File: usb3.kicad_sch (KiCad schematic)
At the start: 45 parts, among them J5 WE_632723300011_alt_symbol, Q4 NX138BKMYL, U17 HD3SS3220, U18 AP22615, U19 TPD4E05U06QDQARQ1, U20 TPD4E05U06QDQARQ1, U21 TPD4E05U06QDQARQ1

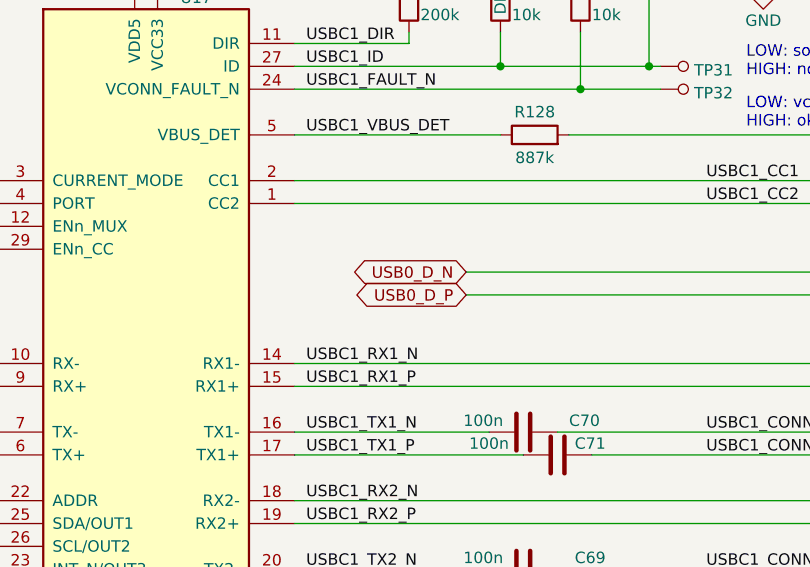
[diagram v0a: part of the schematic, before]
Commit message: Routed USB 2.0; Routed 5V and 3V3 power rails
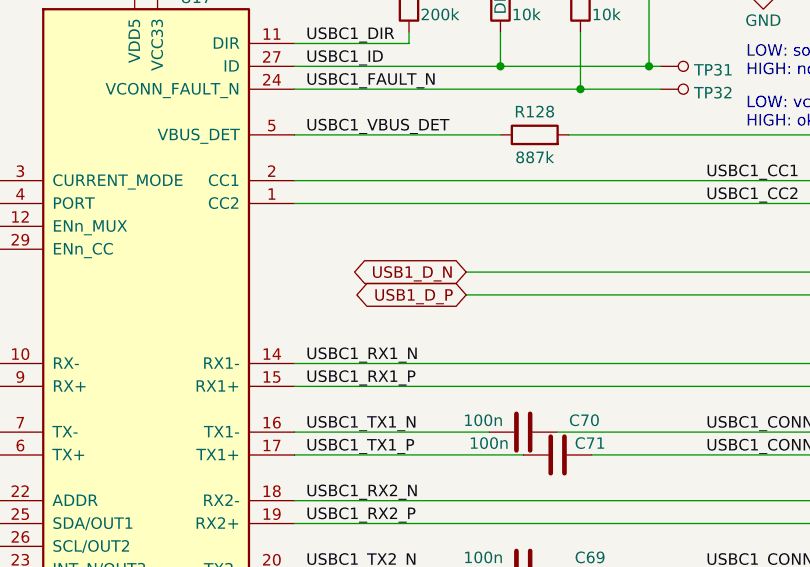
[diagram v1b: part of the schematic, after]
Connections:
- net USB0_D_N renamed USB1_D_N
- net USB0_D_P renamed USB1_D_P
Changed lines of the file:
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@@
-    )
-  )
-  (global_label "USB0_D_P" (shape bidirectional) (at 195.58 147.32 180)
-    (effects (font (size 1.27 1.27)) (justify right))
-    (property "Intersheet References" "${INTERSHEET_REFS}" (id 0) (at 182.245 147.32 0)
-      (effects (font (size 1.1 1.1)) (justify right))
-    )
-  )
-  (global_label "USB0_D_N" (shape bidirectional) (at 195.58 144.78 180)
-    (effects (font (size 1.27 1.27)) (justify right))
-    (property "Intersheet References" "${INTERSHEET_REFS}" (id 0) (at 182.245 144.78 0)
-      (effects (font (size 1.1 1.1)) (justify right))
     )
   )
@@
     )
   )
+  (global_label "USB1_D_N" (shape bidirectional) (at 195.58 144.78 180)
+    (effects (font (size 1.27 1.27)) (justify right))
+    (property "Intersheet References" "${INTERSHEET_REFS}" (id 0) (at 181.5576 144.78 0)
+      (effects (font (size 1.1 1.1)) (justify right))
+    )
+  )
   (global_label "USBSS2_RX_N" (shape output) (at 95.25 154.94 180)
     (effects (font (size 1.27 1.27)) (justify right))
@@
       (effects (font (size 1.1 1.1)) (justify right))
     )
+  )
+  (global_label "USB1_D_P" (shape bidirectional) (at 195.58 147.32 180)
+    (effects (font (size 1.27 1.27)) (justify right))
+    (property "Intersheet References" "${INTERSHEET_REFS}" (id 0) (at 181.61 147.32 0)
+      (effects (font (size 1.1 1.1)) (justify right))
+    )

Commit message: Loclib
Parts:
- C66, C74: footprint antmicro-footprints:0603-cap -> jetson-orin-baseboard-footprints:0603-cap; symbol antmicroCapacitors0603:C_10u_0603 -> jetson-orin-baseboard:C_10u_0603
- C67, C68, C69, C70, C71, C72, C73, C75, C86, C87, C88, C92: footprint antmicro-footprints:0402-cap -> jetson-orin-baseboard-footprints:0402-cap; symbol antmicroCapacitors0402:C_100n_0402 -> jetson-orin-baseboard:C_100n_0402
- D10: footprint antmicro-footprints:SOD-923 -> jetson-orin-baseboard-footprints:SOD-923; symbol antmicroTVSDiodes:ESD9X5.0ST5G -> jetson-orin-baseboard:ESD9X5.0ST5G
- D11: footprint antmicro-footprints:LED_0603 -> jetson-orin-baseboard-footprints:LED_0603; symbol antmicroLEDIndicationDiscrete:LTST-C190GKT -> jetson-orin-baseboard:LTST-C190GKT
- J5: footprint antmicro-footprints:WE_632723300011 -> jetson-orin-baseboard-footprints:WE_632723300011; symbol antmicroUSBDVIHDMIConnectors:WE_632723300011_alt_symbol -> jetson-orin-baseboard:WE_632723300011_alt_symbol
- Q4: footprint antmicro-footprints:DFN1006-3 -> jetson-orin-baseboard-footprints:DFN1006-3; symbol antmicroTransistorsFETsMOSFETsSingle:NX138BKMYL -> jetson-orin-baseboard:NX138BKMYL
- R113, R114, R118, R119, R124, R125: footprint antmicro-footprints:0402-res -> jetson-orin-baseboard-footprints:0402-res; symbol antmicroResistors0402:R_0R_0402 -> jetson-orin-baseboard:R_0R_0402
- R115, R116, R117, R127, R135, R136, R137, R138: footprint antmicro-footprints:0402-res -> jetson-orin-baseboard-footprints:0402-res; symbol antmicroResistors0402:R_10k_0402 -> jetson-orin-baseboard:R_10k_0402
- R126: footprint antmicro-footprints:0402-res -> jetson-orin-baseboard-footprints:0402-res; symbol antmicroResistors0402:R_200k_0402 -> jetson-orin-baseboard:R_200k_0402
- R128: footprint antmicro-footprints:0402-res -> jetson-orin-baseboard-footprints:0402-res; symbol antmicroResistors0402:R_887k_0402 -> jetson-orin-baseboard:R_887k_0402
- R139: footprint antmicro-footprints:0402-res -> jetson-orin-baseboard-footprints:0402-res; symbol antmicroResistors0402:R_2k2_0402 -> jetson-orin-baseboard:R_2k2_0402
- R140: footprint antmicro-footprints:0402-res -> jetson-orin-baseboard-footprints:0402-res; symbol antmicroResistors0402:R_470R_0402 -> jetson-orin-baseboard:R_470R_0402
- TP30, TP31, TP32, TP33: footprint antmicro-footprints:Testpoint_smd_0_75mm -> jetson-orin-baseboard-footprints:Testpoint_smd_0_75mm; symbol antmicroTestPoints:TP_SMD_0_75MM -> jetson-orin-baseboard:TP_SMD_0_75MM
- U17: footprint antmicro-footprints:RNH0030A -> jetson-orin-baseboard-footprints:RNH0030A; symbol antmicroInterfaceControllers:HD3SS3220 -> jetson-orin-baseboard:HD3SS3220
- U18: footprint antmicro-footprints:TSOT23-6 -> jetson-orin-baseboard-footprints:TSOT23-6; symbol antmicroPMICPowerDistributionSwitchesLoadDrivers:AP22615 -> jetson-orin-baseboard:AP22615
- U19, U20, U21: footprint antmicro-footprints:USON-10_2.5x1.0mm_P0.5mm -> jetson-orin-baseboard-footprints:USON-10_2.5x1.0mm_P0.5mm; symbol antmicroTVSDiodes:TPD4E05U06QDQARQ1 -> jetson-orin-baseboard:TPD4E05U06QDQARQ1
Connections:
- net +3V3: no longer U17.8 (VCC33)
- net +5V: no longer U17.30 (VDD5), U18.6 (IN)
- net GND: no longer U17.13 (GND), U17.28 (GND), U17.31 (GND), U18.2 (GND), U20.3 (GND), U20.8 (GND)
- net USBC1_ADDR: no longer U17.22 (ADDR)
- net USBC1_CC1: no longer U17.2 (CC1)
- net USBC1_CC2: no longer U17.1 (CC2)
- net USBC1_CONN_TX1_N: no longer U20.4 (IO3), U20.7 (IO3)
- net USBC1_CONN_TX1_P: no longer U20.5 (IO4), U20.6 (IO4)
- net USBC1_DIR: no longer U17.11 (DIR)
- net USBC1_FAULT_N: no longer U17.24 (VCONN_FAULT_N)
- net USBC1_I2C_SDA: no longer U17.25 (SDA/OUT1)
- net USBC1_ID: no longer U17.27 (ID)
- net USBC1_ISC_SCL: no longer U17.26 (SCL/OUT2)
- net USBC1_ISET: no longer U18.5 (ISET)
- net USBC1_I_MODE: no longer U17.3 (CURRENT_MODE)
- net USBC1_PORT: no longer U17.4 (PORT)
- net USBC1_RX1_N: no longer U17.14 (RX1-), U20.1 (IO1), U20.10 (IO1)
- net USBC1_RX1_P: no longer U17.15 (RX1+), U20.2 (IO2), U20.9 (IO2)
- net USBC1_RX2_N: no longer U17.18 (RX2-)
- net USBC1_RX2_P: no longer U17.19 (RX2+)
- net USBC1_TX1_N: no longer U17.16 (TX1-)
- net USBC1_TX1_P: no longer U17.17 (TX1+)
- net USBC1_TX2_N: no longer U17.20 (TX2-)
- net USBC1_TX2_P: no longer U17.21 (TX2+)
- net USBC1_VBUS: no longer U18.1 (OUT)
- net USBC1_VBUS_DET: no longer U17.5 (VBUS_DET)
- net USBSS1_C_RX_N: no longer U17.10 (RX-)
- net USBSS1_C_RX_P: no longer U17.9 (RX+)
- net USBSS1_C_TX_N: no longer U17.7 (TX-)
- net USBSS1_C_TX_P: no longer U17.6 (TX+)
- net ~{USBC1_EN_CC}: no longer U17.29 (ENn_CC)
- net ~{USBC1_EN_MUX}: no longer U17.12 (ENn_MUX)
- net ~{USBC1_INT}: no longer U17.23 (INT_N/OUT3)
- net at R138.1, TP33.1: no longer U18.3 (FLG)
- net at Q4.3 (D), R137.1: no longer U18.4 (EN)

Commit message: Fix symbols after loclib
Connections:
- net +3V3: now also U17.8 (VCC33)
- net +5V: now also U17.30 (VDD5), U18.6 (IN)
- net GND: now also U17.13 (GND), U17.28 (GND), U17.31 (GND), U18.2 (GND), U20.3 (GND), U20.8 (GND)
- net USBC1_ADDR: now also U17.22 (ADDR)
- net USBC1_CC1: now also U17.2 (CC1)
- net USBC1_CC2: now also U17.1 (CC2)
- net USBC1_CONN_TX1_N: now also U20.4 (IO3), U20.7 (IO3)
- net USBC1_CONN_TX1_P: now also U20.5 (IO4), U20.6 (IO4)
- net USBC1_DIR: now also U17.11 (DIR)
- net USBC1_FAULT_N: now also U17.24 (VCONN_FAULT_N)
- net USBC1_I2C_SDA: now also U17.25 (SDA/OUT1)
- net USBC1_ID: now also U17.27 (ID)
- net USBC1_ISC_SCL: now also U17.26 (SCL/OUT2)
- net USBC1_ISET: now also U18.5 (ISET)
- net USBC1_I_MODE: now also U17.3 (CURRENT_MODE)
- net USBC1_PORT: now also U17.4 (PORT)
- net USBC1_RX1_N: now also U17.14 (RX1-), U20.1 (IO1), U20.10 (IO1)
- net USBC1_RX1_P: now also U17.15 (RX1+), U20.2 (IO2), U20.9 (IO2)
- net USBC1_RX2_N: now also U17.18 (RX2-)
- net USBC1_RX2_P: now also U17.19 (RX2+)
- net USBC1_TX1_N: now also U17.16 (TX1-)
- net USBC1_TX1_P: now also U17.17 (TX1+)
- net USBC1_TX2_N: now also U17.20 (TX2-)
- net USBC1_TX2_P: now also U17.21 (TX2+)
- net USBC1_VBUS: now also U18.1 (OUT)
- net USBC1_VBUS_DET: now also U17.5 (VBUS_DET)
- net USBSS1_C_RX_N: now also U17.10 (RX-)
- net USBSS1_C_RX_P: now also U17.9 (RX+)
- net USBSS1_C_TX_N: now also U17.7 (TX-)
- net USBSS1_C_TX_P: now also U17.6 (TX+)
- net ~{USBC1_EN_CC}: now also U17.29 (ENn_CC)
- net ~{USBC1_EN_MUX}: now also U17.12 (ENn_MUX)
- net ~{USBC1_INT}: now also U17.23 (INT_N/OUT3)
- net at R138.1, TP33.1: now also U18.3 (FLG)
- net at Q4.3 (D), R137.1: now also U18.4 (EN)

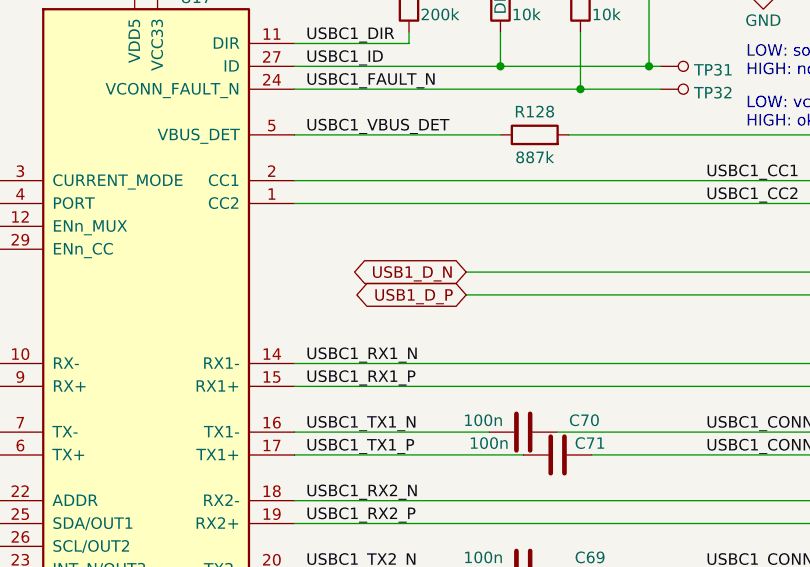
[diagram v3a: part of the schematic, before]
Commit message: Swapped order of USB 2.0 lanes [#40389]
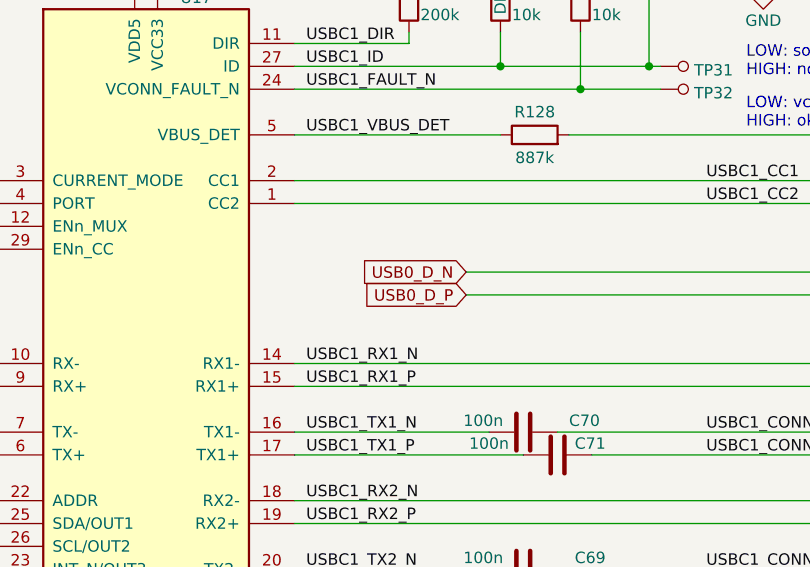
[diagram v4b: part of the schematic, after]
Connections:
- net USB1_D_N renamed USB0_D_N
- net USB1_D_P renamed USB0_D_P
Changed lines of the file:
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@@
+    )
+  )
+  (global_label "USB0_D_N" (shape input) (at 195.58 144.78 180)
+    (effects (font (size 1.27 1.27)) (justify right))
+    (property "Intersheet References" "${INTERSHEET_REFS}" (id 0) (at 182.245 144.78 0)
+      (effects (font (size 1.27 1.27)) (justify right))
     )
   )
@@
     (effects (font (size 1.27 1.27)) (justify right))
     (property "Intersheet References" "${INTERSHEET_REFS}" (id 0) (at 76.835 162.56 0)
+      (effects (font (size 1.27 1.27)) (justify right))
+    )
+  )
+  (global_label "USB0_D_P" (shape input) (at 195.58 147.32 180)
+    (effects (font (size 1.27 1.27)) (justify right))
+    (property "Intersheet References" "${INTERSHEET_REFS}" (id 0) (at 182.245 147.32 0)
       (effects (font (size 1.27 1.27)) (justify right))
     )
@@
     )
   )
-  (global_label "USB1_D_N" (shape bidirectional) (at 195.58 144.78 180)
-    (effects (font (size 1.27 1.27)) (justify right))
-    (property "Intersheet References" "${INTERSHEET_REFS}" (id 0) (at 181.5576 144.78 0)
-      (effects (font (size 1.1 1.1)) (justify right))
-    )
-  )
   (global_label "USBSS2_RX_N" (shape output) (at 95.25 154.94 180)
     (effects (font (size 1.27 1.27)) (justify right))
@@
       (effects (font (size 1.1 1.1)) (justify right))
     )
-  )
-  (global_label "USB1_D_P" (shape bidirectional) (at 195.58 147.32 180)
-    (effects (font (size 1.27 1.27)) (justify right))
-    (property "Intersheet References" "${INTERSHEET_REFS}" (id 0) (at 181.61 147.32 0)
-      (effects (font (size 1.1 1.1)) (justify right))
-    )

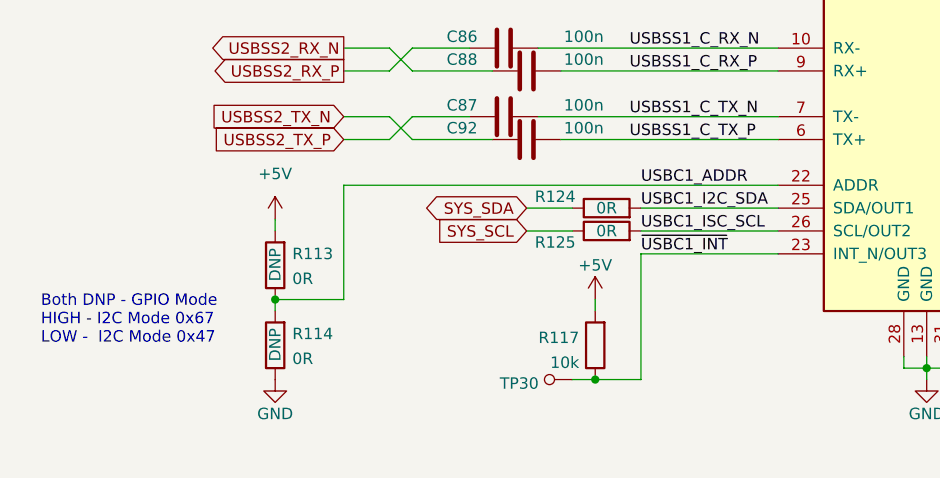
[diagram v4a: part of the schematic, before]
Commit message: Changed default configuration of U17 to I2C [#40390]
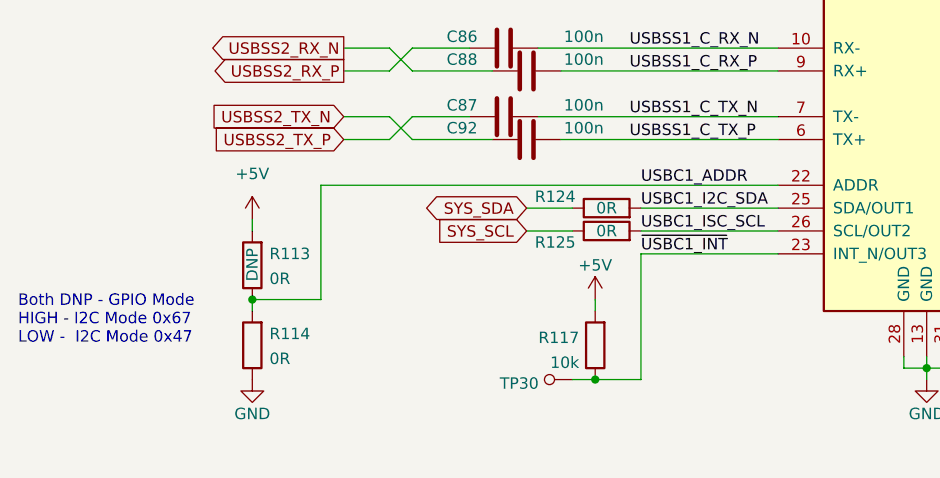
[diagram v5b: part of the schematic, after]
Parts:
- R114: DNP DNP -> (none)
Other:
- moved on the sheet: R113, R114
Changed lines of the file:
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@@
   (junction (at 245.11 177.8) (diameter 0) (color 0 0 0 0)
   )
-  (junction (at 87.63 182.88) (diameter 0) (color 0 0 0 0)
+  (junction (at 85.09 182.88) (diameter 0) (color 0 0 0 0)
   )
   (junction (at 123.19 191.77) (diameter 0) (color 0 0 0 0)
@@
     (stroke (width 0) (type default) (color 0 0 0 0))
   )
-  (wire (pts (xy 87.63 182.88) (xy 87.63 184.15))
+  (wire (pts (xy 85.09 182.88) (xy 85.09 184.15))
     (stroke (width 0) (type default) (color 0 0 0 0))
   )
@@
     (stroke (width 0) (type default) (color 0 0 0 0))
   )
-  (wire (pts (xy 95.25 182.88) (xy 95.25 170.18))
+  (wire (pts (xy 92.71 182.88) (xy 92.71 170.18))
     (stroke (width 0) (type default) (color 0 0 0 0))
   )
@@
     (stroke (width 0) (type default) (color 0 0 0 0))
   )
-  (wire (pts (xy 87.63 182.88) (xy 95.25 182.88))
+  (wire (pts (xy 85.09 182.88) (xy 92.71 182.88))
     (stroke (width 0) (type default) (color 0 0 0 0))
   )
-  (wire (pts (xy 95.25 170.18) (xy 143.51 170.18))
+  (wire (pts (xy 92.71 170.18) (xy 143.51 170.18))
     (stroke (width 0) (type default) (color 0 0 0 0))
   )
@@
     (stroke (width 0) (type default) (color 0 0 0 0))
   )
-  (wire (pts (xy 87.63 173.99) (xy 87.63 175.26))
+  (wire (pts (xy 85.09 173.99) (xy 85.09 175.26))
     (stroke (width 0) (type default) (color 0 0 0 0))
   )
@@
   )
   (text "Both DNP - GPIO Mode\nHIGH - I2C Mode 0x67\nLOW -  I2C Mode 0x47"
-    (at 61.595 187.96 0)
+    (at 59.055 187.96 0)
     (effects (font (size 1.27 1.27)) (justify left bottom))
   )
@@
     (pin "1")
   )
-  (symbol (lib_id "jetson-orin-baseboard:R_0R_0402") (at 87.63 187.96 90) (unit 1)
+  (symbol (lib_id "jetson-orin-baseboard:R_0R_0402") (at 85.09 187.96 90) (unit 1)
     (in_bom yes) (on_board yes)
-    (property "Reference" "R114" (id 0) (at 89.535 186.69 90)
+    (property "Reference" "R114" (id 0) (at 86.995 186.69 90)
       (effects (font (size 1.27 1.27)) (justify right))
     )
-    (property "Value" "R_0R_0402" (id 1) (at 91.44 187.96 0)
+    (property "Value" "R_0R_0402" (id 1) (at 88.9 187.96 0)
       (effects (font (size 1.27 1.27)) hide)
     )
-    (property "Footprint" "jetson-orin-baseboard-footprints:0402-res" (id 2) (at 82.55 182.88 0)
+    (property "Footprint" "jetson-orin-baseboard-footprints:0402-res" (id 2) (at 80.01 182.88 0)
       (effects (font (size 1.524 1.524)) (justify left) hide)
     )
-    (property "Datasheet" "" (id 3) (at 87.63 187.96 0)
+    (property "Datasheet" "" (id 3) (at 85.09 187.96 0)
       (effects (font (size 1.27 1.27)) hide)
     )
-    (property "Manufacturer" "PANASONIC" (id 4) (at 77.47 182.88 0)
+    (property "Manufacturer" "PANASONIC" (id 4) (at 74.93 182.88 0)
       (effects (font (size 1.524 1.524)) (justify left) hide)
     )
-    (property "MPN" "ERJ2GE0R00X" (id 5) (at 80.01 182.88 0)
+    (property "MPN" "ERJ2GE0R00X" (id 5) (at 77.47 182.88 0)
       (effects (font (size 1.524 1.524)) (justify left) hide)
     )
-    (property "Val" "0R" (id 6) (at 89.535 189.4551 90)
-      (effects (font (size 1.27 1.27)) (justify right))
-    )
-    (property "DNP" "DNP" (id 7) (at 87.63 186.055 0)
+    (property "Val" "0R" (id 6) (at 86.995 189.4551 90)
       (effects (font (size 1.27 1.27)) (justify right))
     )
@@
     (pin "1")
   )
-  (symbol (lib_id "jetson-orin-baseboard:GND") (at 87.63 191.77 0) (unit 1)
+  (symbol (lib_id "jetson-orin-baseboard:GND") (at 85.09 191.77 0) (unit 1)
     (in_bom yes) (on_board yes)
-    (property "Reference" "#PWR0109" (id 0) (at 87.63 198.12 0)
+    (property "Reference" "#PWR0109" (id 0) (at 85.09 198.12 0)
       (effects (font (size 1.27 1.27)) hide)
     )
-    (property "Value" "GND" (id 1) (at 87.63 195.58 0))
-    (property "Footprint" "" (id 2) (at 87.63 191.77 0)
+    (property "Value" "GND" (id 1) (at 85.09 195.58 0))
+    (property "Footprint" "" (id 2) (at 85.09 191.77 0)
       (effects (font (size 1.27 1.27)) hide)
     )
-    (property "Datasheet" "" (id 3) (at 87.63 191.77 0)
+    (property "Datasheet" "" (id 3) (at 85.09 191.77 0)
       (effects (font (size 1.27 1.27)) hide)
     )
@@
     (pin "2")
   )
-  (symbol (lib_id "jetson-orin-baseboard:+5V") (at 87.63 173.99 0) (unit 1)
+  (symbol (lib_id "jetson-orin-baseboard:+5V") (at 85.09 173.99 0) (unit 1)
     (in_bom yes) (on_board yes) (fields_autoplaced)
-    (property "Reference" "#PWR0108" (id 0) (at 87.63 177.8 0)
+    (property "Reference" "#PWR0108" (id 0) (at 85.09 177.8 0)
       (effects (font (size 1.27 1.27)) hide)
     )
-    (property "Value" "+5V" (id 1) (at 87.63 168.91 0))
-    (property "Footprint" "" (id 2) (at 87.63 173.99 0)
+    (property "Value" "+5V" (id 1) (at 85.09 168.91 0))
+    (property "Footprint" "" (id 2) (at 85.09 173.99 0)
       (effects (font (size 1.27 1.27)) hide)
     )
-    (property "Datasheet" "" (id 3) (at 87.63 173.99 0)
+    (property "Datasheet" "" (id 3) (at 85.09 173.99 0)
       (effects (font (size 1.27 1.27)) hide)
     )
@@
     (pin "1")
   )
-  (symbol (lib_id "jetson-orin-baseboard:R_0R_0402") (at 87.63 179.07 90) (unit 1)
+  (symbol (lib_id "jetson-orin-baseboard:R_0R_0402") (at 85.09 179.07 90) (unit 1)
     (in_bom yes) (on_board yes)
-    (property "Reference" "R113" (id 0) (at 89.535 177.8 90)
+    (property "Reference" "R113" (id 0) (at 86.995 177.8 90)
       (effects (font (size 1.27 1.27)) (justify right))
     )
-    (property "Value" "R_0R_0402" (id 1) (at 91.44 179.07 0)
+    (property "Value" "R_0R_0402" (id 1) (at 88.9 179.07 0)
       (effects (font (size 1.27 1.27)) hide)
     )
-    (property "Footprint" "jetson-orin-baseboard-footprints:0402-res" (id 2) (at 82.55 173.99 0)
+    (property "Footprint" "jetson-orin-baseboard-footprints:0402-res" (id 2) (at 80.01 173.99 0)
       (effects (font (size 1.524 1.524)) (justify left) hide)
     )
-    (property "Datasheet" "" (id 3) (at 87.63 179.07 0)
+    (property "Datasheet" "" (id 3) (at 85.09 179.07 0)
       (effects (font (size 1.27 1.27)) hide)
     )
-    (property "Manufacturer" "PANASONIC" (id 4) (at 77.47 173.99 0)
+    (property "Manufacturer" "PANASONIC" (id 4) (at 74.93 173.99 0)
       (effects (font (size 1.524 1.524)) (justify left) hide)
     )
-    (property "MPN" "ERJ2GE0R00X" (id 5) (at 80.01 173.99 0)
+    (property "MPN" "ERJ2GE0R00X" (id 5) (at 77.47 173.99 0)
       (effects (font (size 1.524 1.524)) (justify left) hide)
     )
-    (property "Val" "0R" (id 6) (at 89.535 180.5651 90)
+    (property "Val" "0R" (id 6) (at 86.995 180.5651 90)
       (effects (font (size 1.27 1.27)) (justify right))
     )
-    (property "DNP" "DNP" (id 7) (at 87.63 177.165 0)
+    (property "DNP" "DNP" (id 7) (at 85.09 177.165 0)
       (effects (font (size 1.27 1.27)) (justify right))
     )
